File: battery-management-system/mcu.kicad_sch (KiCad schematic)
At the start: 46 parts, among them J15 MCU_SUPPLY, J16 I2C, J17 UART_INTERCONNECT, J18 LEDS, J19 CHARGE/DISCHARGE, J20 UART_USB, Q5 DMN3730U, U10 STC3100, U11 STM32L071CZTx, U7 ARM-JTAG-SWD, U8 AT24C512C, U9 NCT75DR2G

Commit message: improve layout
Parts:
- removed J15: MCU_SUPPLY, benediktibk:PinHeader_1x03_P2.54mm_Vertical, symbol benediktibk:Conn_01x03
- removed R58: 2mOhm, benediktibk:R_2512_6332Metric_Pad1.40x3.35mm_HandSolder, symbol benediktibk:R_2mOhm_SMD_2512_5W_1%
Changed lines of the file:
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@@
   (junction (at 36.83 137.16) (diameter 0) (color 0 0 0 0)
   )
-  (junction (at 41.91 31.75) (diameter 0) (color 0 0 0 0)
-  )
   (junction (at 182.88 104.14) (diameter 0) (color 0 0 0 0)
   )
@@
   )
   (junction (at 36.83 186.69) (diameter 0) (color 0 0 0 0)
-  )
-  (junction (at 33.02 31.75) (diameter 0) (color 0 0 0 0)
   )
   (junction (at 74.93 135.89) (diameter 0) (color 0 0 0 0)
@@
     (stroke (width 0) (type default))
   )
-  (wire (pts (xy 40.64 31.75) (xy 41.91 31.75))
-    (stroke (width 0) (type default))
-  )
   (wire (pts (xy 64.77 31.75) (xy 64.77 36.83))
     (stroke (width 0) (type default))
@@
     (stroke (width 0) (type default))
   )
-  (wire (pts (xy 35.56 22.86) (xy 41.91 22.86))
-    (stroke (width 0) (type default))
-  )
   (wire (pts (xy 116.84 44.45) (xy 116.84 46.99))
     (stroke (width 0) (type default))
@@
     (stroke (width 0) (type default))
   )
-  (wire (pts (xy 33.02 22.86) (xy 33.02 31.75))
-    (stroke (width 0) (type default))
-  )
-  (wire (pts (xy 22.86 31.75) (xy 33.02 31.75))
-    (stroke (width 0) (type default))
-  )
-  (wire (pts (xy 30.48 22.86) (xy 30.48 25.4))
-    (stroke (width 0) (type default))
-  )
   (wire (pts (xy 205.74 109.22) (xy 205.74 113.03))
     (stroke (width 0) (type default))
@@
     (stroke (width 0) (type default))
   )
-  (wire (pts (xy 41.91 22.86) (xy 41.91 31.75))
-    (stroke (width 0) (type default))
-  )
   (wire (pts (xy 129.54 31.75) (xy 129.54 36.83))
     (stroke (width 0) (type default))
@@
     (stroke (width 0) (type default))
   )
-  (wire (pts (xy 41.91 31.75) (xy 53.34 31.75))
+  (wire (pts (xy 30.48 31.75) (xy 53.34 31.75))
     (stroke (width 0) (type default))
   )
@@
     (effects (font (size 1.27 1.27)) (justify left))
   )
-  (hierarchical_label "3V3" (shape input) (at 22.86 31.75 180) (fields_autoplaced)
+  (hierarchical_label "3V3" (shape input) (at 30.48 31.75 180) (fields_autoplaced)
     (effects (font (size 1.27 1.27)) (justify right))
   )
@@
         (path "/5272f0ff-3069-41a9-bca2-80beede8b4b2/409f87d1-afa6-40d2-ba42-d5009501b8f9"
           (reference "#PWR055") (unit 1)
-        )
-      )
-    )
-  )
-  (symbol (lib_id "benediktibk:Conn_01x03") (at 33.02 17.78 270) (mirror x) (unit 1)
-    (in_bom yes) (on_board yes) (dnp no)
-    (property "Reference" "J15" (at 38.1 13.97 90)
-      (effects (font (size 1.27 1.27)))
-    )
-    (property "Value" "MCU_SUPPLY" (at 27.94 13.97 90)
-      (effects (font (size 1.27 1.27)))
-    )
-    (property "Footprint" "benediktibk:PinHeader_1x03_P2.54mm_Vertical" (at 33.02 17.78 0)
-      (effects (font (size 1.27 1.27)) hide)
-    )
-    (property "Datasheet" "~" (at 33.02 17.78 0)
-      (effects (font (size 1.27 1.27)) hide)
-    )
-    (property "RS order number" "251-8092" (at 33.02 17.78 0)
-      (effects (font (size 1.27 1.27)) hide)
-    )
-    (pin "1")
-    (pin "2")
-    (pin "3")
-    (instances
-      (project "battery-management-system"
-        (path "/5272f0ff-3069-41a9-bca2-80beede8b4b2/409f87d1-afa6-40d2-ba42-d5009501b8f9"
-          (reference "J15") (unit 1)
         )
       )
@@
     )
   )
-  (symbol (lib_id "benediktibk:R_2mOhm_SMD_2512_5W_1%") (at 36.83 31.75 90) (unit 1)
-    (in_bom yes) (on_board yes) (dnp no)
-    (property "Reference" "R58" (at 43.18 35.56 90)
-      (effects (font (size 1.27 1.27)))
-    )
-    (property "Value" "2mOhm" (at 36.83 35.56 90)
-      (effects (font (size 1.27 1.27)))
-    )
-    (property "Footprint" "benediktibk:R_2512_6332Metric_Pad1.40x3.35mm_HandSolder" (at 36.322 41.91 90)
-      (effects (font (size 1.27 1.27)) hide)
-    )
-    (property "Datasheet" "~" (at 36.83 31.75 0)
-      (effects (font (size 1.27 1.27)) hide)
-    )
-    (property "RS order number" "231-3683" (at 35.56 49.53 0)
-      (effects (font (size 1.27 1.27)) hide)
-    )
-    (pin "1")
-    (pin "2")
-    (instances
-      (project "battery-management-system"
-        (path "/5272f0ff-3069-41a9-bca2-80beede8b4b2/b1377397-46a1-4623-af59-88e4e694ca35"
-          (reference "R58") (unit 1)
-        )
-        (path "/5272f0ff-3069-41a9-bca2-80beede8b4b2/409f87d1-afa6-40d2-ba42-d5009501b8f9"
-          (reference "R28") (unit 1)
-        )
-      )
-    )
-  )
   (symbol (lib_id "power:GND") (at 96.52 99.06 0) (unit 1)
     (in_bom yes) (on_board yes) (dnp no) (fields_autoplaced)
@@
         )
       )
-    )
-  )
-  (symbol (lib_id "power:GND") (at 30.48 25.4 0) (unit 1)
-    (in_bom yes) (on_board yes) (dnp no) (fields_autoplaced)
-    (property "Reference" "#PWR047" (at 30.48 31.75 0)
-      (effects (font (size 1.27 1.27)) hide)
-    )
-    (property "Value" "GND" (at 33.02 26.67 0)
-      (effects (font (size 1.27 1.27)) (justify left))
-    )
-    (property "Footprint" "" (at 30.48 25.4 0)
-      (effects (font (size 1.27 1.27)) hide)
-    )
-    (property "Datasheet" "" (at 30.48 25.4 0)
-      (effects (font (size 1.27 1.27)) hide)
-    )
-    (pin "1")
-    (instances
-      (project "battery-management-system"
-        (path "/5272f0ff-3069-41a9-bca2-80beede8b4b2/409f87d1-afa6-40d2-ba42-d5009501b8f9"
-          (reference "#PWR047") (unit 1)
-        )
-      )

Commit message: finish routing
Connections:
- net CELL_BALANCING_A0: now also U11.45 (PB8); no longer U11.25 (PB12)
- net CELL_BALANCING_A1: now also U11.46 (PB9); no longer U11.26 (PB13)
- net CHARGE: now also U11.39 (PB3); no longer U11.27 (PB14)
- net CHARGE_AVAILABLE: now also U11.28 (PB15); no longer U11.18 (PB0)
- net DISCHARGE: now also U11.38 (PA15); no longer U11.28 (PB15)
- net EN_CELL_BALANCING: now also U11.40 (PB4); no longer U11.33 (PA12)
- net LED1: now also U11.2 (PC13); no longer U11.17 (PA7)
- net LED2: now also U11.3 (PC14); no longer U11.29 (PA8)
- net LED3: now also U11.4 (PC15); no longer U11.32 (PA11)
- net LIMIT_BALANCING_CURRENT: now also U11.41 (PB5); no longer U11.38 (PA15)
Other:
- moved on the sheet: J19

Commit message: add project for DC DC converter PCB
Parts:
- RESET1: RS order number 244-4461 -> 244-4461
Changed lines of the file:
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@@
       (effects (font (size 1.27 1.27)) hide)
     )
-    (property "RS order number" " 244-4461" (at 83.82 88.9 0)
+    (property "RS order number" "244-4461" (at 83.82 88.9 0)
       (effects (font (size 0 0)) hide)
     )

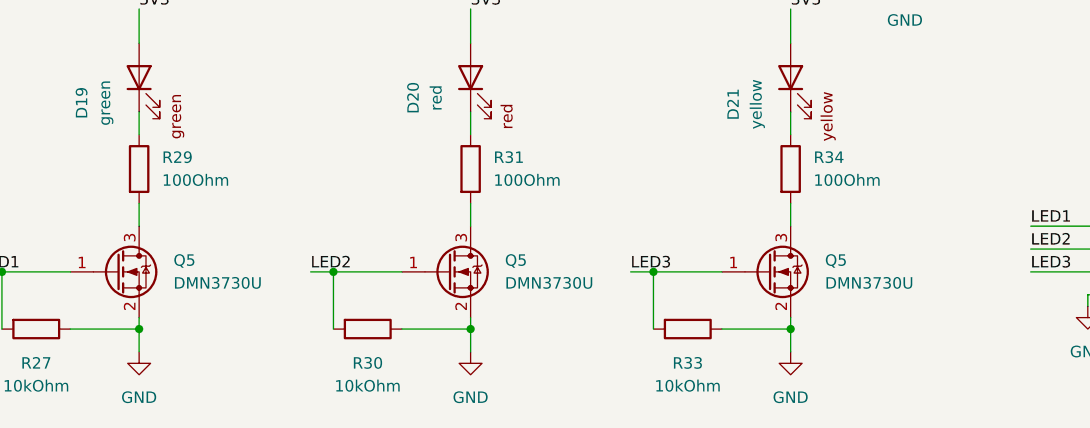
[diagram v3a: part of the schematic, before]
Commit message: switch to inductor based cell balancing
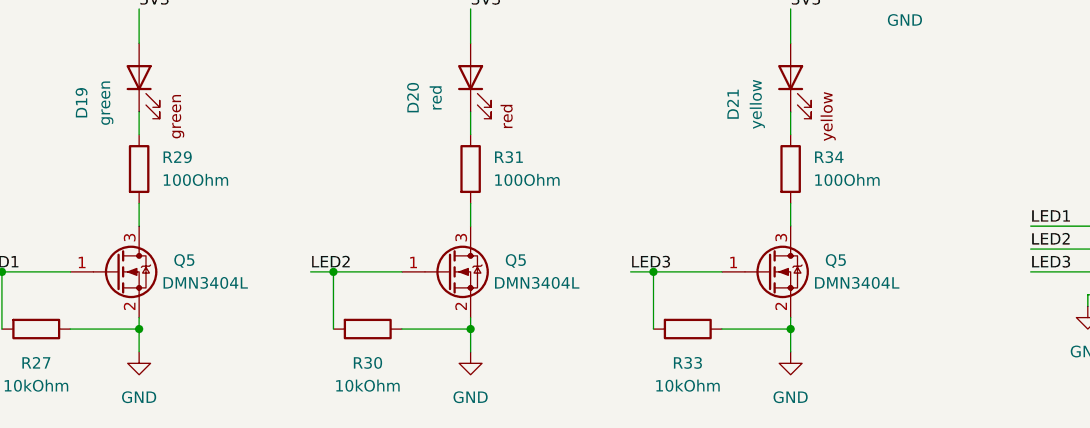
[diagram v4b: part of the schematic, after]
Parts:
- Q5: value DMN3730U -> DMN3404L; symbol benediktibk:DMN3730U -> benediktibk:DMN3404L; RS order number 823-2946 -> 751-4171
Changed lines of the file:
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@@
     )
   )
-  (symbol (lib_id "benediktibk:DMN3730U") (at 34.29 180.34 0) (unit 1)
+  (symbol (lib_id "benediktibk:DMN3404L") (at 34.29 180.34 0) (unit 1)
     (in_bom yes) (on_board yes) (dnp no)
     (property "Reference" "Q5" (at 40.64 179.0699 0)
       (effects (font (size 1.27 1.27)) (justify left))
     )
-    (property "Value" "DMN3730U" (at 40.64 181.6099 0)
+    (property "Value" "DMN3404L" (at 39.37 181.61 0)
       (effects (font (size 1.27 1.27)) (justify left))
     )
@@
       (effects (font (size 1.27 1.27)) hide)
     )
-    (property "RS order number" "823-2946" (at 31.75 185.42 0)
+    (property "RS order number" "751-4171" (at 31.75 185.42 0)
       (effects (font (size 1.27 1.27)) hide)
     )
@@
     )
   )
-  (symbol (lib_id "benediktibk:DMN3730U") (at 106.68 180.34 0) (unit 1)
+  (symbol (lib_id "benediktibk:DMN3404L") (at 106.68 180.34 0) (unit 1)
     (in_bom yes) (on_board yes) (dnp no)
     (property "Reference" "Q5" (at 113.03 179.0699 0)
       (effects (font (size 1.27 1.27)) (justify left))
     )
-    (property "Value" "DMN3730U" (at 113.03 181.6099 0)
+    (property "Value" "DMN3404L" (at 111.76 181.61 0)
       (effects (font (size 1.27 1.27)) (justify left))
     )
@@
       (effects (font (size 1.27 1.27)) hide)
     )
-    (property "RS order number" "823-2946" (at 104.14 185.42 0)
+    (property "RS order number" "751-4171" (at 104.14 185.42 0)
       (effects (font (size 1.27 1.27)) hide)
     )
@@
     )
   )
-  (symbol (lib_id "benediktibk:DMN3730U") (at 71.12 180.34 0) (unit 1)
+  (symbol (lib_id "benediktibk:DMN3404L") (at 71.12 180.34 0) (unit 1)
     (in_bom yes) (on_board yes) (dnp no)
     (property "Reference" "Q5" (at 77.47 179.0699 0)
       (effects (font (size 1.27 1.27)) (justify left))
     )
-    (property "Value" "DMN3730U" (at 77.47 181.6099 0)
+    (property "Value" "DMN3404L" (at 76.2 181.61 0)
       (effects (font (size 1.27 1.27)) (justify left))
     )
@@
       (effects (font (size 1.27 1.27)) hide)
     )
-    (property "RS order number" "823-2946" (at 68.58 185.42 0)
-      (effects (font (size 1.27 1.27)) hide)
-    )
+    (property "RS order number" "751-4171" (at 68.58 185.42 0)
+      (effects (font (size 1.27 1.27)) hide)
+    )
